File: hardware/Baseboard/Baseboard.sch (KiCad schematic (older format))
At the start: 0 parts

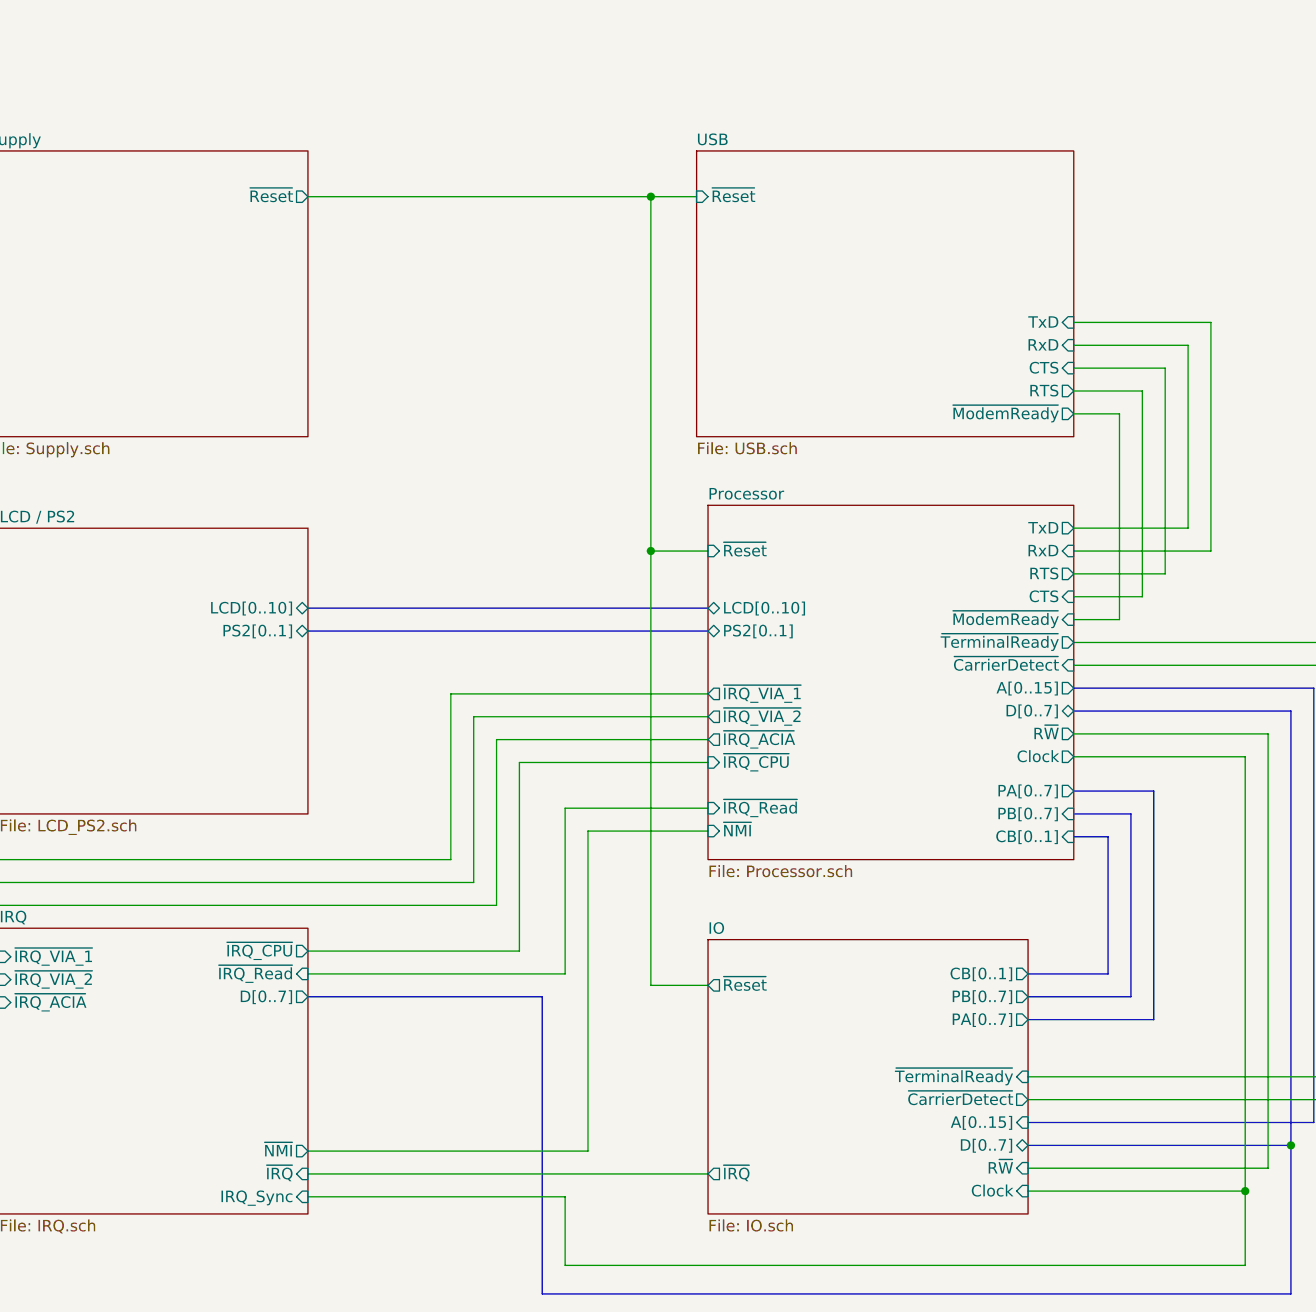
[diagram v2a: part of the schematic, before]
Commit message: Optimize routing, add RDY and SYNC to expansion header
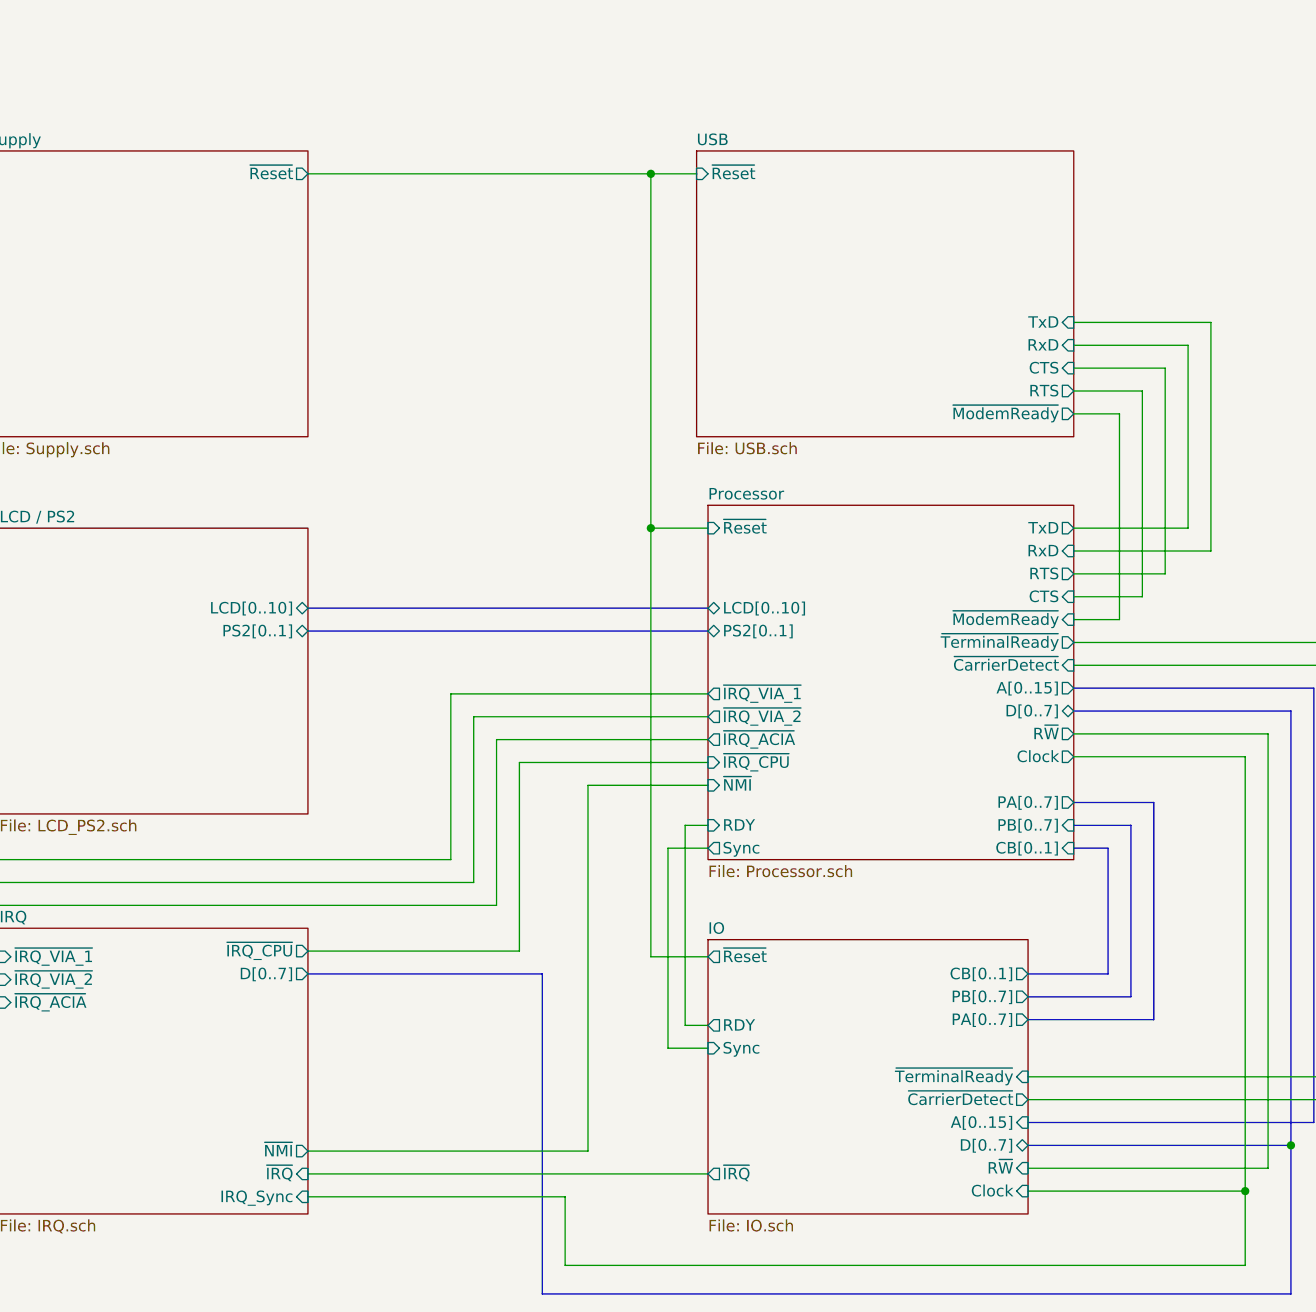
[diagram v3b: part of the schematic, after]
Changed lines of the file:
@@
 Text Notes 3250 1100 0    150  ~ 30
 Memory map
-Wire Wire Line
-	6500 4900 8000 4900
-Wire Wire Line
-	8250 6450 8000 6450
-Wire Wire Line
-	8000 6450 8000 4900
-Connection ~ 8000 4900
-Wire Wire Line
-	8000 4900 8200 4900
 $Sheet
 S 5100 4700 1400 1250
@@
 F0 "Supply" 50
 F1 "Supply.sch" 50
-F2 "~Reset" O R 6500 4900 50
+F2 "~Reset" O R 6500 4800 50
 $EndSheet
 Wire Bus Line
 	9650 8300 10000 8300
 Wire Bus Line
-	10000 8300 10000 7700
-Wire Bus Line
-	10000 7700 9850 7700
+	10000 8300 10000 7750
 $Sheet
 S 8250 8150 1400 1200
@@
 F7 "~TerminalReady" I R 9650 8750 50
 F8 "~CarrierDetect" O R 9650 8850 50
-F9 "~Reset" O L 8250 8350 50
+F9 "~Reset" O L 8250 8225 50
 F10 "CB[0..1]" O R 9650 8300 50
 F11 "A[0..15]" I R 9650 8950 50
 F12 "D[0..7]" B R 9650 9050 50
+F13 "RDY" O L 8250 8525 50
+F14 "Sync" I L 8250 8625 50
 $EndSheet
 Text Notes 900  1850 0    100  ~ 0
@@
 F0 "Processor" 50
 F1 "Processor.sch" 50
-F2 "PA[0..7]" O R 9850 7500 50
-F3 "PB[0..7]" I R 9850 7600 50
+F2 "PA[0..7]" O R 9850 7550 50
+F3 "PB[0..7]" I R 9850 7650 50
 F4 "TxD" O R 9850 6350 50
 F5 "RxD" I R 9850 6450 50
 F6 "RTS" O R 9850 6550 50
 F7 "CTS" I R 9850 6650 50
-F8 "~NMI" I L 8250 7675 50
+F8 "~NMI" I L 8250 7475 50
 F9 "R~W" O R 9850 7250 50
 F10 "LCD[0..10]" B L 8250 6700 50
@@
 F14 "~TerminalReady" O R 9850 6850 50
 F15 "~CarrierDetect" I R 9850 6950 50
-F16 "~Reset" I L 8250 6450 50
+F16 "~Reset" I L 8250 6350 50
 F17 "~IRQ_VIA_2" O L 8250 7175 50
 F18 "~IRQ_VIA_1" O L 8250 7075 50
 F19 "~IRQ_ACIA" O L 8250 7275 50
 F20 "~IRQ_CPU" I L 8250 7375 50
-F21 "~IRQ_Read" I L 8250 7575 50
-F22 "CB[0..1]" I R 9850 7700 50
-F23 "A[0..15]" O R 9850 7050 50
-F24 "D[0..7]" B R 9850 7150 50
+F21 "CB[0..1]" I R 9850 7750 50
+F22 "A[0..15]" O R 9850 7050 50
+F23 "D[0..7]" B R 9850 7150 50
+F24 "RDY" I L 8250 7650 50
+F25 "Sync" O L 8250 7750 50
 $EndSheet
 Wire Bus Line
@@
 Wire Wire Line
 	10600 9250 9650 9250
-Connection ~ 8000 6450
-Wire Wire Line
-	8250 8350 8000 8350
-Wire Wire Line
-	8000 6450 8000 8350
 Wire Bus Line
 	6500 6800 8250 6800
@@
 F5 "RTS" O R 9850 5750 50
 F6 "~ModemReady" O R 9850 5850 50
-F7 "~Reset" I L 8200 4900 50
-$EndSheet
-Wire Bus Line
-	9850 7600 10100 7600
-Wire Bus Line
-	9850 7500 10200 7500
+F7 "~Reset" I L 8200 4800 50
+$EndSheet
 Wire Wire Line
 	10600 7350 10600 9250
@@
 	9650 8400 10100 8400
 Wire Bus Line
-	10100 8400 10100 7600
+	10100 8400 10100 7650
 Wire Bus Line
 	9650 8500 10200 8500
 Wire Bus Line
-	10200 8500 10200 7500
+	10200 8500 10200 7550
 Wire Wire Line
 	11100 6850 11100 8750
@@
 F6 "~IRQ_CPU" O R 6500 8200 50
 F7 "IRQ_Sync" I R 6500 9275 50
-F8 "~IRQ_Read" I R 6500 8300 50
-F9 "D[0..7]" O R 6500 8400 50
-F10 "~NMI" O R 6500 9075 50
+F8 "D[0..7]" O R 6500 8300 50
+F9 "~NMI" O R 6500 9075 50
 $EndSheet
 Wire Wire Line
@@
 	7325 8000 5075 8000
 Wire Wire Line
-	7625 7575 8250 7575
-Wire Wire Line
 	8250 9175 6500 9175
 Wire Wire Line
@@
 	7425 7375 7425 8200
 Wire Wire Line
-	7625 7575 7625 8300
-Wire Wire Line
 	5150 8425 5075 8425
 Wire Wire Line
@@
 Wire Wire Line
 	6500 9075 7725 9075
-Wire Wire Line
-	8250 7675 7725 7675
-Wire Wire Line
-	7725 7675 7725 9075
-Wire Bus Line
-	6500 8400 7525 8400
-Wire Bus Line
-	7525 8400 7525 9700
-Wire Wire Line
-	6500 8300 7625 8300
 Wire Wire Line
 	10600 9250 10600 9575
@@
 	7625 9275 6500 9275
 Connection ~ 10600 9250
+Wire Bus Line
+	6500 8300 7525 8300
+Wire Bus Line
+	7525 8300 7525 9700
+Wire Bus Line
+	9850 7550 10200 7550
+Wire Bus Line
+	9850 7650 10100 7650
+Wire Bus Line
+	9850 7750 10000 7750
+Wire Wire Line
+	8250 7475 7725 7475
+Wire Wire Line
+	7725 7475 7725 9075
+Wire Wire Line
+	8075 8625 8250 8625
+Wire Wire Line
+	8250 7750 8075 7750
+Wire Wire Line
+	8075 7750 8075 8625
+Wire Wire Line
+	8250 7650 8150 7650
+Wire Wire Line
+	8150 7650 8150 8525
+Wire Wire Line
+	8150 8525 8250 8525
+Wire Wire Line
+	8250 8225 8000 8225
+Wire Wire Line
+	8250 6350 8000 6350
+Connection ~ 8000 6350
+Wire Wire Line
+	8000 6350 8000 8225
+Wire Wire Line
+	6500 4800 8000 4800
+Wire Wire Line
+	8000 4800 8000 6350
+Connection ~ 8000 4800
+Wire Wire Line
+	8000 4800 8200 4800
 $EndSCHEMATC

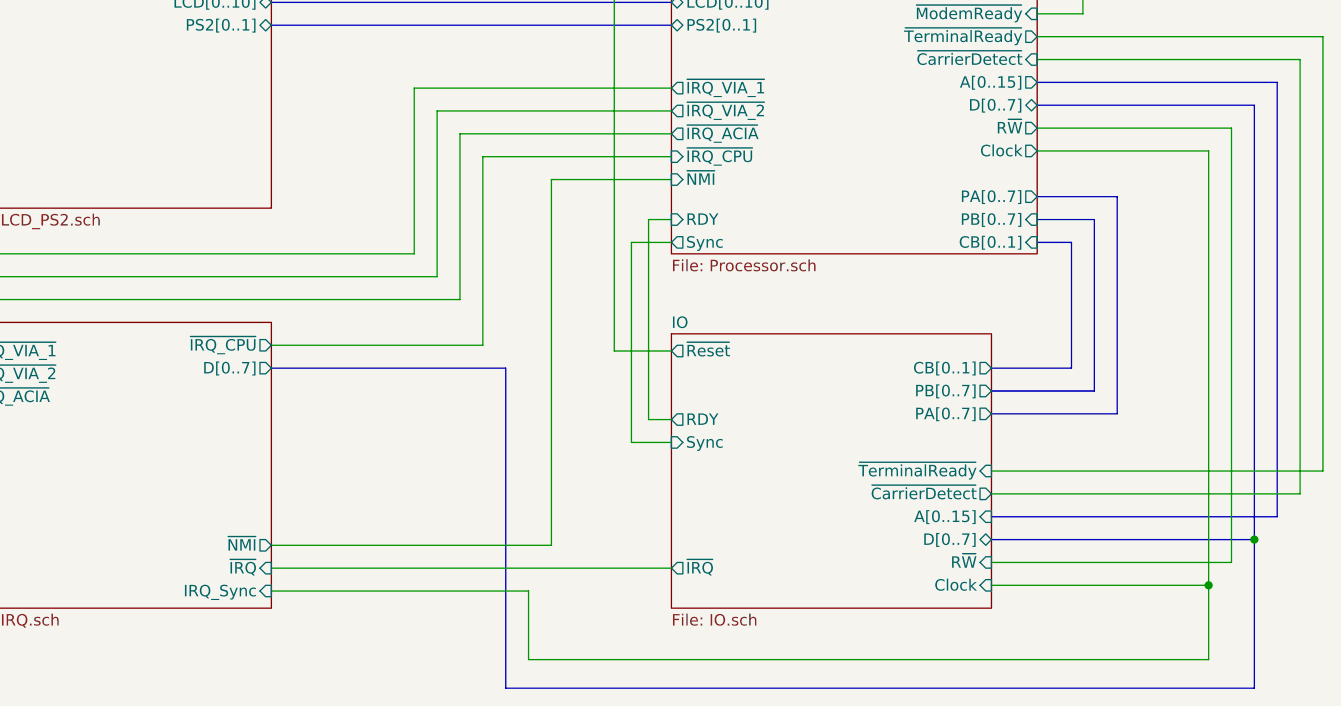
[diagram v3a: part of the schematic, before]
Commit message: Add VP signal to expansion header, optimize routing
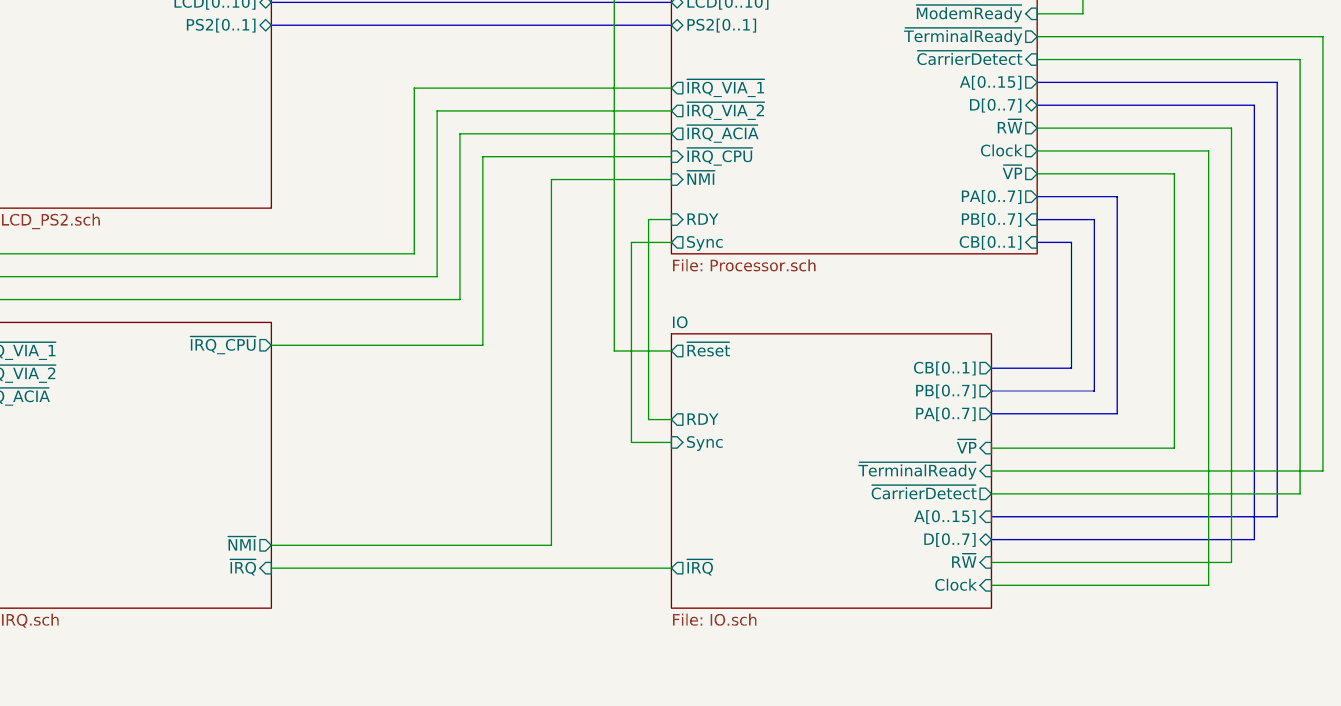
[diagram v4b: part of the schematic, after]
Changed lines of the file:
@@
 F13 "RDY" O L 8250 8525 50
 F14 "Sync" I L 8250 8625 50
+F15 "~VP" I R 9650 8650 50
 $EndSheet
 Text Notes 900  1850 0    100  ~ 0
@@
 F24 "RDY" I L 8250 7650 50
 F25 "Sync" O L 8250 7750 50
+F26 "~VP" O R 9850 7450 50
 $EndSheet
 Wire Bus Line
@@
 F5 "~IRQ_ACIA" I L 5150 8425 50
 F6 "~IRQ_CPU" O R 6500 8200 50
-F7 "IRQ_Sync" I R 6500 9275 50
-F8 "D[0..7]" O R 6500 8300 50
-F9 "~NMI" O R 6500 9075 50
+F7 "~NMI" O R 6500 9075 50
 $EndSheet
 Wire Wire Line
 	8250 7375 7425 7375
-Wire Bus Line
-	10800 9050 10800 9700
-Wire Bus Line
-	10800 9700 7525 9700
-Connection ~ 10800 9050
 Wire Wire Line
 	8250 7075 7125 7075
@@
 Wire Wire Line
 	6500 9075 7725 9075
-Wire Wire Line
-	10600 9250 10600 9575
-Wire Wire Line
-	10600 9575 7625 9575
-Wire Wire Line
-	7625 9575 7625 9275
-Wire Wire Line
-	7625 9275 6500 9275
-Connection ~ 10600 9250
-Wire Bus Line
-	6500 8300 7525 8300
-Wire Bus Line
-	7525 8300 7525 9700
 Wire Bus Line
 	9850 7550 10200 7550
@@
 Wire Wire Line
 	8000 4800 8200 4800
+Wire Wire Line
+	9850 7450 10450 7450
+Wire Wire Line
+	10450 7450 10450 8650
+Wire Wire Line
+	10450 8650 9650 8650
 $EndSCHEMATC

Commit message: Working on PCB
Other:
- note removed: "Select:"
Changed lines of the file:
@@
 Sheet 1 7
 Title "Baseboard"
-Date "2019-11-24"
-Rev "1.1"
+Date "2020-01-17"
+Rev "1.0"
 Comp "https://www.kampis-elektroecke.de"
 Comment1 "Author: Daniel Kampert"
@@
 Text Notes 3550 2100 0    100  ~ 0
 SRAM
-Text Notes 5600 1450 0    100  ~ 20
-Select:
 Wire Notes Line width 18 style solid
 	5350 1150 5350 3700
-Text Notes 3250 1100 0    150  ~ 30
+Text Notes 2275 1075 0    150  ~ 30
 Memory map
 $Sheet
@@
 F1 "Supply.sch" 50
 F2 "~Reset" O R 6500 4800 50
+F3 "~Reset_FT232" O R 6500 4900 50
 $EndSheet
 Wire Bus Line
@@
 F5 "R~W" I R 9650 9150 50
 F6 "Clock" I R 9650 9250 50
-F7 "~TerminalReady" I R 9650 8750 50
-F8 "~CarrierDetect" O R 9650 8850 50
-F9 "~Reset" O L 8250 8225 50
-F10 "CB[0..1]" O R 9650 8300 50
-F11 "A[0..15]" I R 9650 8950 50
-F12 "D[0..7]" B R 9650 9050 50
-F13 "RDY" O L 8250 8525 50
-F14 "Sync" I L 8250 8625 50
-F15 "~VP" I R 9650 8650 50
+F7 "~Reset" O L 8250 8225 50
+F8 "CB[0..1]" O R 9650 8300 50
+F9 "A[0..15]" I R 9650 8950 50
+F10 "D[0..7]" B R 9650 9050 50
+F11 "RDY" O L 8250 8525 50
+F12 "Sync" I L 8250 8625 50
+F13 "~VP" I R 9650 8650 50
+F14 "~DCD" O R 9650 8850 50
 $EndSheet
 Text Notes 900  1850 0    100  ~ 0
 $0000 - $FFFF\n
 Wire Notes Line width 18 style solid
-	750  1550 6700 1550
-Wire Notes Line width 18 style solid
-	750  1150 6700 1150
-Wire Notes Line width 18 style solid
-	6700 1150 6700 3700
+	750  1550 5350 1550
+Wire Notes Line width 18 style solid
+	750  1150 5350 1150
 Wire Notes Line width 18 style solid
 	750  1150 750  3700
 Wire Wire Line
-	9850 5450 10450 5450
-Wire Wire Line
-	10350 5550 9850 5550
-Wire Wire Line
-	9850 5650 10250 5650
-Wire Wire Line
-	10250 5650 10250 6550
-Wire Wire Line
-	10250 6550 9850 6550
-Wire Wire Line
-	10150 5750 9850 5750
-Wire Wire Line
-	9850 5850 10050 5850
-Wire Wire Line
-	10050 5850 10050 6750
-Wire Wire Line
-	10050 6750 9850 6750
+	9850 5375 10450 5375
+Wire Wire Line
+	10350 5475 9850 5475
+Wire Wire Line
+	9850 5575 10250 5575
+Wire Wire Line
+	10150 6550 9850 6550
+Wire Wire Line
+	9850 5775 10050 5775
 Wire Wire Line
 	9850 6350 10350 6350
 Wire Wire Line
-	10350 6350 10350 5550
+	10350 6350 10350 5475
 Wire Wire Line
 	9850 6450 10450 6450
@@
 24K
 Wire Wire Line
-	10450 5450 10450 6450
+	10450 5375 10450 6450
 $Sheet
 S 5150 6350 1350 1250
@@
 F4 "TxD" O R 9850 6350 50
 F5 "RxD" I R 9850 6450 50
-F6 "RTS" O R 9850 6550 50
-F7 "CTS" I R 9850 6650 50
-F8 "~NMI" I L 8250 7475 50
-F9 "R~W" O R 9850 7250 50
-F10 "LCD[0..10]" B L 8250 6700 50
-F11 "PS2[0..1]" B L 8250 6800 50
-F12 "~ModemReady" I R 9850 6750 50
-F13 "Clock" O R 9850 7350 50
-F14 "~TerminalReady" O R 9850 6850 50
-F15 "~CarrierDetect" I R 9850 6950 50
-F16 "~Reset" I L 8250 6350 50
-F17 "~IRQ_VIA_2" O L 8250 7175 50
-F18 "~IRQ_VIA_1" O L 8250 7075 50
-F19 "~IRQ_ACIA" O L 8250 7275 50
-F20 "~IRQ_CPU" I L 8250 7375 50
-F21 "CB[0..1]" I R 9850 7750 50
-F22 "A[0..15]" O R 9850 7050 50
-F23 "D[0..7]" B R 9850 7150 50
-F24 "RDY" I L 8250 7650 50
-F25 "Sync" O L 8250 7750 50
-F26 "~VP" O R 9850 7450 50
+F6 "~NMI" I L 8250 7475 50
+F7 "R~W" O R 9850 7250 50
+F8 "LCD[0..10]" B L 8250 6700 50
+F9 "PS2[0..1]" B L 8250 6800 50
+F10 "Clock" O R 9850 7350 50
+F11 "~Reset" I L 8250 6350 50
+F12 "~IRQ_VIA_2" O L 8250 7175 50
+F13 "~IRQ_VIA_1" O L 8250 7075 50
+F14 "~IRQ_ACIA" O L 8250 7275 50
+F15 "~IRQ_CPU" I L 8250 7375 50
+F16 "CB[0..1]" I R 9850 7750 50
+F17 "A[0..15]" O R 9850 7050 50
+F18 "D[0..7]" B R 9850 7150 50
+F19 "RDY" I L 8250 7650 50
+F20 "Sync" O L 8250 7750 50
+F21 "~VP" O R 9850 7450 50
+F22 "~RTS" O R 9850 6550 50
+F23 "~CTS" I R 9850 6650 50
+F24 "~DSR" I R 9850 6850 50
+F25 "~DTR" O R 9850 6750 50
+F26 "~DCD" I R 9850 6950 50
 $EndSheet
 Wire Bus Line
@@
 	8250 6700 6500 6700
 Wire Wire Line
-	10150 6650 10150 5750
-Wire Wire Line
-	9850 6650 10150 6650
-$Sheet
-S 8200 4700 1650 1250
-U 5E9064F2
-F0 "USB" 50
-F1 "USB.sch" 50
-F2 "TxD" I R 9850 5450 50
-F3 "RxD" I R 9850 5550 50
-F4 "CTS" I R 9850 5650 50
-F5 "RTS" O R 9850 5750 50
-F6 "~ModemReady" O R 9850 5850 50
-F7 "~Reset" I L 8200 4800 50
-$EndSheet
-Wire Wire Line
 	10600 7350 10600 9250
 Wire Bus Line
@@
 Wire Bus Line
 	10200 8500 10200 7550
-Wire Wire Line
-	11100 6850 11100 8750
-Wire Wire Line
-	9850 6850 11100 6850
-Wire Wire Line
-	9650 8750 11100 8750
-Wire Wire Line
-	9650 8850 11000 8850
-Wire Wire Line
-	11000 8850 11000 6950
-Wire Wire Line
-	11000 6950 9850 6950
 $Sheet
 S 5150 8100 1350 1250
@@
 Wire Wire Line
 	8000 4800 8000 6350
-Connection ~ 8000 4800
-Wire Wire Line
-	8000 4800 8200 4800
-Wire Wire Line
-	9850 7450 10450 7450
-Wire Wire Line
-	10450 7450 10450 8650
-Wire Wire Line
-	10450 8650 9650 8650
+Wire Wire Line
+	9850 7450 10475 7450
+Wire Wire Line
+	10475 7450 10475 8650
+Wire Wire Line
+	10475 8650 9650 8650
+$Sheet
+S 8200 4700 1650 1250
+U 5E9064F2
+F0 "USB" 50
+F1 "USB.sch" 50
+F2 "RxD" I R 9850 5475 50
+F3 "~CTS" I R 9850 5675 50
+F4 "~RTS" O R 9850 5575 50
+F5 "~DTR" O R 9850 5775 50
+F6 "~DSR" I R 9850 5875 50
+F7 "TxD" O R 9850 5375 50
+F8 "~Reset_FT232" I L 8200 4900 50
+$EndSheet
+Wire Wire Line
+	9850 5875 9950 5875
+Wire Wire Line
+	9950 5875 9950 6750
+Wire Wire Line
+	9850 6950 11000 6950
+Wire Wire Line
+	11000 6950 11000 8850
+Wire Wire Line
+	11000 8850 9650 8850
+Wire Wire Line
+	10150 5675 10150 6550
+Wire Wire Line
+	9850 5675 10150 5675
+Wire Wire Line
+	10250 5575 10250 6650
+Wire Wire Line
+	9850 6650 10250 6650
+Wire Wire Line
+	10050 5775 10050 6850
+Wire Wire Line
+	9850 6750 9950 6750
+Wire Wire Line
+	9850 6850 10050 6850
+Wire Wire Line
+	6500 4900 8200 4900
 $EndSCHEMATC
